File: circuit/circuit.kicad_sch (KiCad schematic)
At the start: 24 parts, among them SW1 SW_Push_DPDT, U1 NJM4558, U2 NJM5532, U3 NJM5532

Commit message: add : REAMDE.md
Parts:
- R10, R6: value 4.7k -> 45k
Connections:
- net GND: now also U1.6 (-)
- net at U1.1, U1.5 (+): no longer U1.6 (-)
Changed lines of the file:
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@@
 	)
 	(junction
-		(at 95.25 38.1)
+		(at 114.3 76.2)
 		(diameter 0)
 		(color 0 0 0 0)
 	)
 	(junction
-		(at 114.3 76.2)
+		(at 95.25 45.72)
 		(diameter 0)
 		(color 0 0 0 0)
@@
 	(wire
 		(pts
+			(xy 95.25 45.72) (xy 119.38 45.72)
+		)
+		(stroke
+			(width 0)
+			(type default)
+		)
+	)
+	(wire
+		(pts
 			(xy 129.54 38.1) (xy 133.35 38.1)
 		)
@@
 	(wire
 		(pts
-			(xy 110.49 66.04) (xy 114.3 66.04)
+			(xy 95.25 40.64) (xy 95.25 45.72)
 		)
 		(stroke
@@
 	(wire
 		(pts
-			(xy 76.2 63.5) (xy 77.47 63.5)
+			(xy 110.49 66.04) (xy 114.3 66.04)
 		)
 		(stroke
@@
 	(wire
 		(pts
-			(xy 168.91 105.41) (xy 166.37 105.41)
+			(xy 76.2 63.5) (xy 77.47 63.5)
 		)
 		(stroke
@@
 	(wire
 		(pts
-			(xy 129.54 38.1) (xy 129.54 40.64)
+			(xy 168.91 105.41) (xy 166.37 105.41)
 		)
 		(stroke
@@
 	(wire
 		(pts
-			(xy 114.3 86.36) (xy 114.3 88.9)
+			(xy 129.54 38.1) (xy 129.54 40.64)
 		)
 		(stroke
@@
 	(wire
 		(pts
-			(xy 72.39 45.72) (xy 119.38 45.72)
+			(xy 114.3 86.36) (xy 114.3 88.9)
 		)
 		(stroke
@@
 	(wire
 		(pts
-			(xy 95.25 38.1) (xy 95.25 40.64)
+			(xy 72.39 45.72) (xy 95.25 45.72)
 		)
 		(stroke
@@
 			)
 		)
-		(property "Value" "4.7k"
+		(property "Value" "45k"
 			(at 116.84 124.4599 0)
 			(effects
@@
 			)
 		)
-		(property "Value" "4.7k"
+		(property "Value" "45k"
 			(at 116.84 83.8199 0)
 			(effects

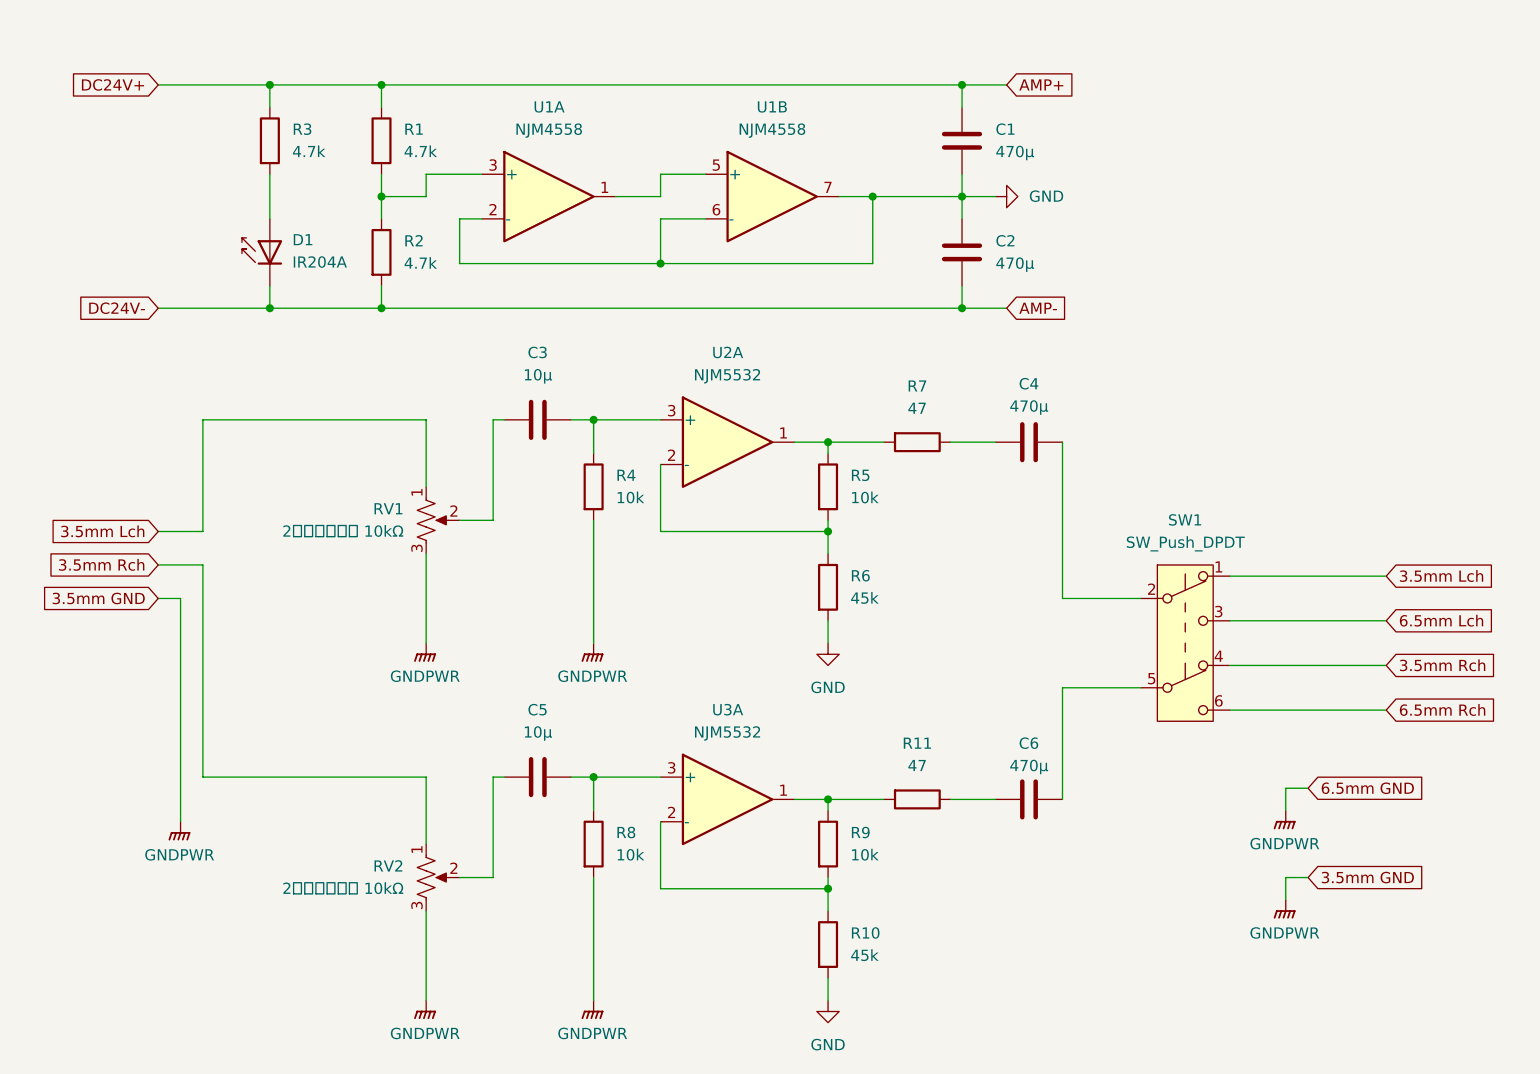
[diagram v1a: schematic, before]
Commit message: add : ユニバーサル基板のレイアウト
その他回路図の間違いを修正
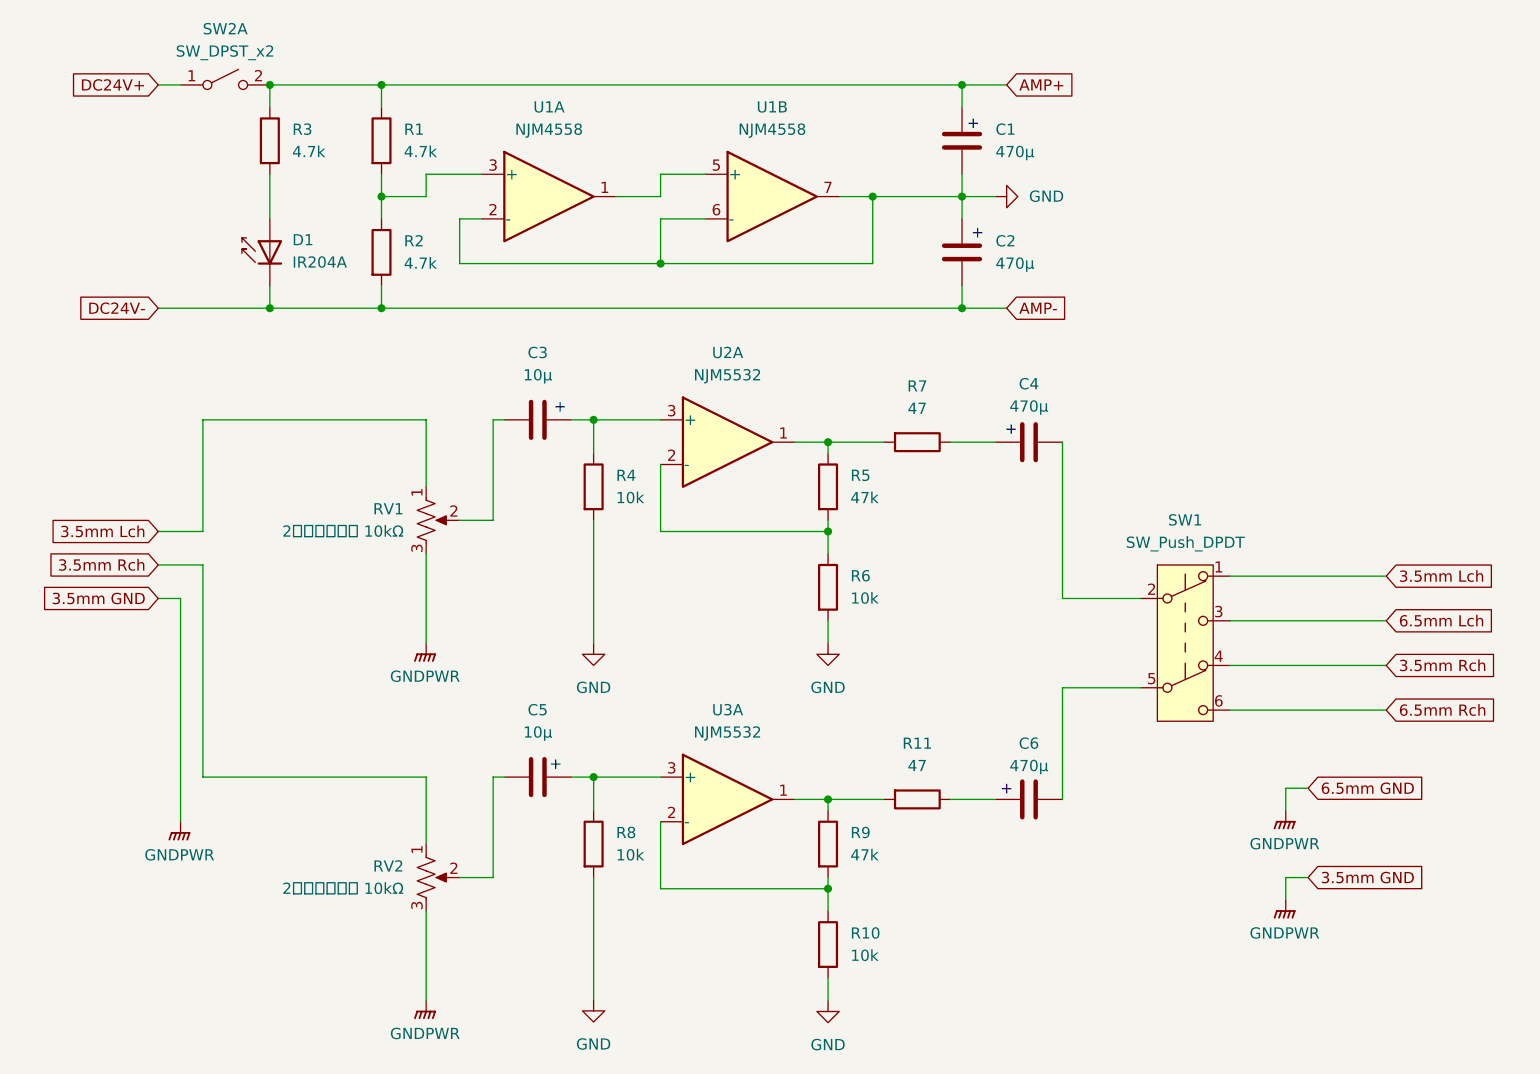
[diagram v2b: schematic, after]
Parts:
- added SW2: SW_DPST_x2, symbol Switch:SW_DPST_x2
- R10, R6: value 45k -> 10k
- R5, R9: value 10k -> 47k
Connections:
- net AMP+: now also SW2.2 (B)
- net GND: now also R4.2, R8.2
- net GNDPWR: no longer R4.2, R8.2
- new net DC24V+: SW2.1 (A)
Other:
- note added: "+"

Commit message: update : power circuit
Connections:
- net AMP- is gone; now on net GND: C2.2, D1.1 (K), R2.2
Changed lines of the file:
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@@
+	)
+	(symbol
+		(lib_id "power:GND")
+		(at 129.54 50.8 0)
+		(unit 1)
+		(exclude_from_sim no)
+		(in_bom yes)
+		(on_board yes)
+		(dnp no)
+		(fields_autoplaced yes)
+		(property "Reference" "#PWR011"
+			(at 129.54 57.15 0)
+			(effects
+				(font
+					(size 1.27 1.27)
+				)
+				(hide yes)
+			)
+		)
+		(property "Value" "GND"
+			(at 129.54 55.88 0)
+			(effects
+				(font
+					(size 1.27 1.27)
+				)
+			)
+		)
+		(property "Footprint" ""
+			(at 129.54 50.8 0)
+			(effects
+				(font
+					(size 1.27 1.27)
+				)
+				(hide yes)
+			)
+		)
+		(property "Datasheet" ""
+			(at 129.54 50.8 0)
+			(effects
+				(font
+					(size 1.27 1.27)
+				)
+				(hide yes)
+			)
+		)
+		(property "Description" "Power symbol creates a global label with name \"GND\" , ground"
+			(at 129.54 50.8 0)
+			(effects
+				(font
+					(size 1.27 1.27)
+				)
+				(hide yes)
+			)
+		)
+		(pin "1"
+		)
+		(instances
+			(project "circuit"
+				(path "/c737c3f8-550a-435a-8d91-74b4d65c537a"
+					(reference "#PWR011")
+					(unit 1)
+				)
+			)
+		)
 	)
 	(symbol

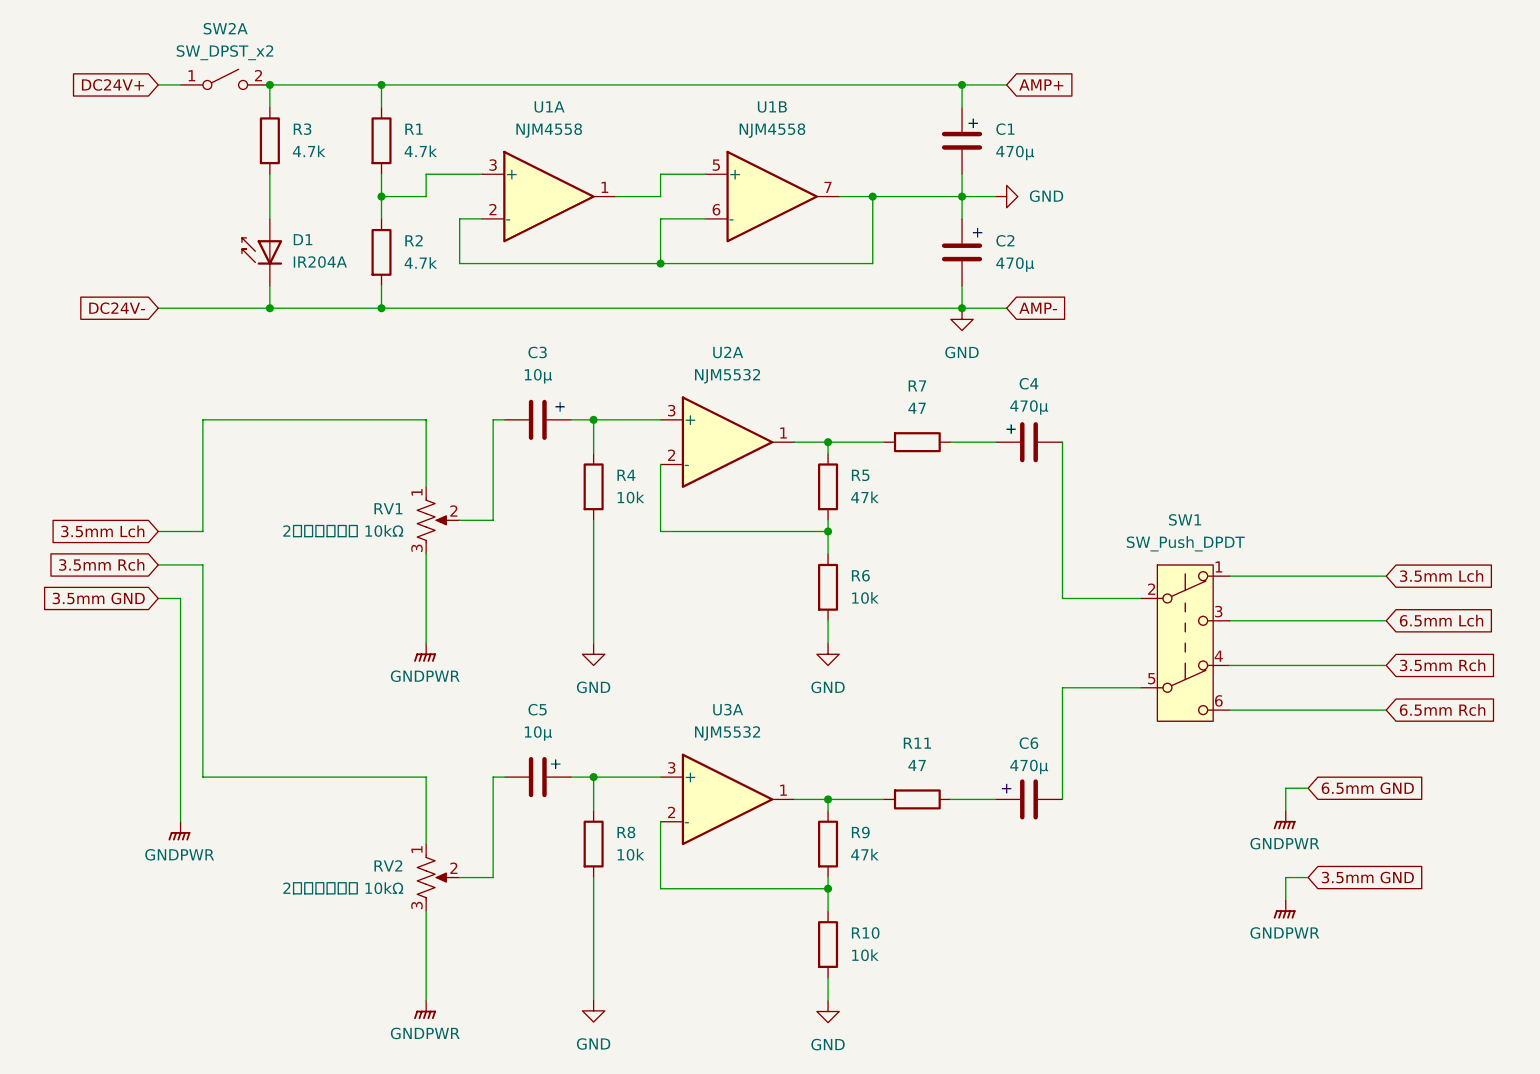
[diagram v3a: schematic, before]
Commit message: add : case part
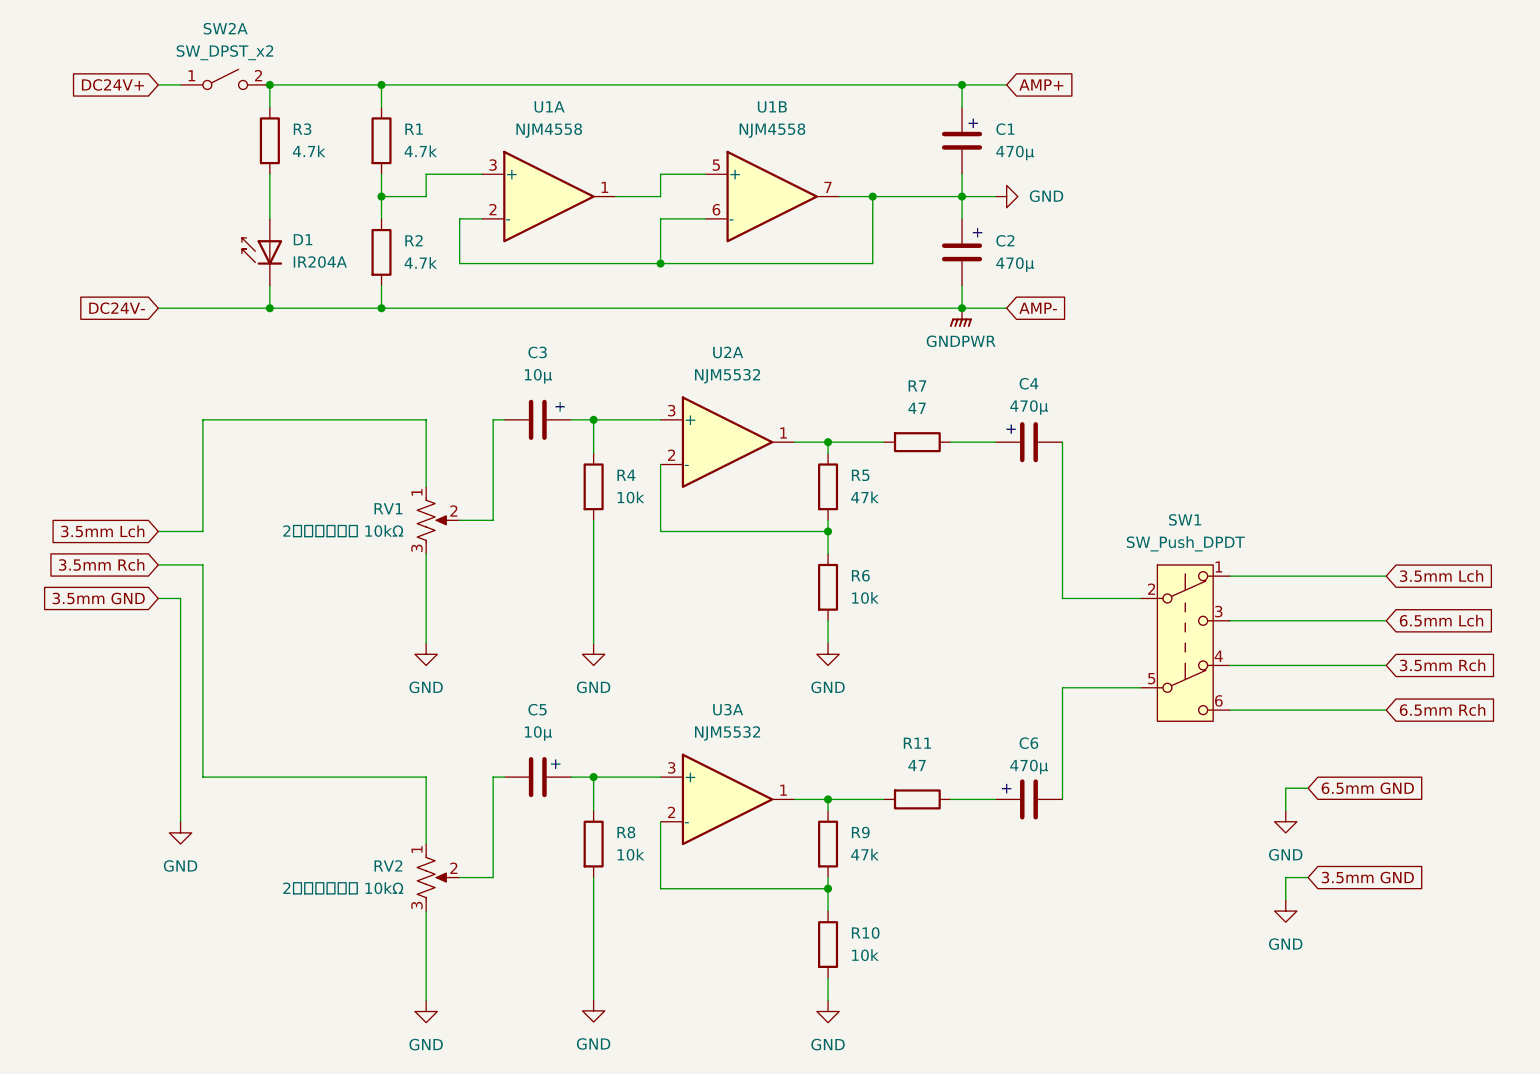
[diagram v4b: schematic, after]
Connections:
- net GND: now also RV1.3, RV2.3; no longer C2.2, D1.1 (K), R2.2
- net GNDPWR: now also C2.2, D1.1 (K), R2.2; no longer RV1.3, RV2.3
